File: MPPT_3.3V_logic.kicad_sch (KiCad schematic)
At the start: 42 parts, among them Q1 SIR5607DP-T1-RE3, Q2 SIR5607DP-T1-RE3, Q3 SIR5607DP-T1-RE3, Q4 SIR5607DP-T1-RE3, U1 LTC4417HUF, U2 TPS259470ARPWR, U3 TPS62177DQCR

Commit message: Started layout of the Ideal diode input (LTC4417)
I'm considering getting rid of the second 3V3 buck but will need to weigh the pros and cons a little more before commiting
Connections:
- net Solar_+X renamed OR'd_VOUT
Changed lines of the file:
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@@
 			"QQBLAE0AaABLAEEAQQBBAEEAQQBBAEEAQQBGAEcAUQBsAEEAQQBBAEEAQQBBAEEAQQBDAHIASQBT"
 			"AEEAQQBBAEEAQQBBAEEAQQBCAFYAawBKAEEAQQBBAEEAQQBBAEMAQQBnAHEAdwBFAEEAQQBBAEEA"
-			"QQBBAEIAQQBRAFYAWQBDAEEAQQBBAEEAQQBBAEMAZwBJAEMAcwBCAEEAQQBBAEEAQQBBAEIAUQ=="
+			"QQBBAEIAQQBRAFYAWQBDAEEAQQBBAEEAQQBBAEMAZwBJAEMAcwBCAEEAQQBBAEEAQQBBAEIAUQAv"
+			"AFEASQAyAGMAbgArAGYAQQBMAFAAQQBBAGcAQgBhAEQAVgBrAEoAQQBBAEEAQQBFAEUANgBUAC8A"
+			"bQBtAHkALwB3AHIAQgBFADYAWQAvAGYAbQArADMAZQB4AHMAVgBqAHAAdwA4AEsAaQA0ACsAcgBs"
+			"AEgAaABvAEoASABKAFMAUQA4AC8AZQBBAHYANwBCAHcAQwA0AG0AVQA1AEwAbAB5ADUAdAA2AHoA"
+			"NgBnAC8AYgBwAHkAOQBjAHAAWAAzADMAegBWADEAcgAwAEEAQQBBAEQAbwBTAEwAcgBlADAAMwBY"
+			"AFEAcQBPAFIATABGAHkANQBkAHYAWABKAFYAUgBPADcAdgBjAC8AOAAvAC8AUABDAHAAQgAxAE0A"
+			"RwArAE4AZQBNADYAQgBTAGgASABUADMANABlAHUAMQAxADEAMgBWAFgAegBkAFcAYQA3AGoAMgA3"
+			"AGoALwBvAEgALwBXAFAAZgBlADYAegBWAHUAdwB5AGcAOQBRAHoAdABPADEAVABWAHUAWABHAGMA"
+			"aQB2AGIAbQByAHUAdgBYAHIANwBkADEASAA5AEIAKwBuAGIAdAA0AGYAcwBPAG4ARwA5AHEANgBG"
+			"AHcAQQBBAEEAQQBCAHcAbQA1AGgAcABlAEUANQA5AHQANwBxAHQAZQA0AEcAYgA0AEIANABjAEEA"
+			"QQBBAEEAQQBBAEEAQQBCAFYAawBKAEEAQQBBAEEAQQBBAEMAQQBnAHEAdwBFAEEAQQBBAEEAQQBB"
+			"AEIAQQBRAFYAWQBDAEEAQQBBAEEAQQBBAEMAZwBpAEcAegByAEQAZwBBAEEAQQBBAEMAMwBvAFcA"
+			"cABuAGQAYwBXAHgAOABoAHAAWABUAFcAeQB2ADcAdgA0AEwAQQA5AGQAWAA0ADcAcABhAGYAcQB6"
+			"AGkANAB2AGsATAAzAFQAVAAzADkAZQBqAGQASQA3AEkAegBmADYASQBEAFEAQgB2AGoASAAyAEkA"
+			"QQBBAEEAQQBnAHoARAA3AGIAdABzAGYAeQB3AFMANQAzAGoAZAB2AHoAdABQACsAUQB4AE0AbgBQ"
+			"AEcAYQBQAFUAVQBmADQAMQBqAHgANABvAC8AVwBqAEQAWAB5ACsAYwB2ACsAQgA1AEcAdABNAGoA"
+			"NQBzAGsAZgBQAGQAVwBqADkALwAyAHQAMQAxAGMAQQBnAEIALwB1AHcAUQBFAEEAQQBBAEQAQwB5"
+			"AGYATABoAHIAaAAxAC8ALwByAFEAdQBLAEIARwBSAG8AdwBkAEsALwA3ADUAbABwADMALwBOAFEA"
+			"LwB1ACsALwB1AEEAUAA3ADkAYwBGAEoAUwBKAFMAZQBiAHIAUwB2AFAARwBUAHkAdABPAFYAcg=="
 		)
 	)
@@
 		)
 	)
-	(hierarchical_label "Solar_+X"
+	(hierarchical_label "OR'd_VOUT"
 		(shape input)
 		(at 33.02 95.25 180)

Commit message: Efuses for this board and Battery board
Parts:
- removed L1: 10uH, zLibrary:IND_BOURNS_SRR6038, symbol Device:L
- removed U3: TPS62177DQCR, zLibrary:DQC0010A, symbol TPS62177:TPS62175DQCR
- added R19, R20, R21: 100k, Resistor_SMD:R_0603_1608Metric, symbol Device:R
- added R22, R23: 10k, Resistor_SMD:R_0805_2012Metric, symbol Device:R
- added U3: TPS259470ARPWR, zLibrary:RPW0010A-MFG, symbol TPS259470:TPS259470ARPWR
- C10: value 100pF -> 2.2nF; MANUFACTURER_PART_NUMBER 885342206001 -> GCM1885C1H222FA16D
- C11: value 1uF -> 2.2nF; MANUFACTURER_PART_NUMBER CL10B105KQ8NNNC -> GCM1885C1H222FA16D
- C12: value 22uF -> 100pF; footprint zLibrary:CAP_C2220C_2S_KEM-M -> Capacitor_SMD:C_0603_1608Metric; MANUFACTURER_PART_NUMBER C2220C226MMR2L7289 -> 885342206001
- C13: value 100nF -> 100pF; MANUFACTURER_PART_NUMBER 06035C104K4T2A -> 885342206001
- C14, C15: value 22uF -> 10uF; footprint zLibrary:CAP_C2220C_2S_KEM-M -> Capacitor_SMD:C_1206_3216Metric; MANUFACTURER_PART_NUMBER C2220C226MMR2L7289 -> AVX, 04025C104KAT2A
- C9: value 2.2nF -> 100nF; MANUFACTURER_PART_NUMBER GCM1885C1H222FA16D -> 06035C104K4T2A
- R14: value 350k -> 182k; MANUFACTURER Digikey -> (none); MANUFACTURER_PART_NUMBER RN73R1JTTD3483F25 -> (none)
- R15, R18: value 100k -> 20k; MANUFACTURER Digikey -> (none); MANUFACTURER_PART_NUMBER AT0603FRE07100KL -> (none)
- R16: value 5k -> 100k; MANUFACTURER_PART_NUMBER RN73R1JTTD4991F100 -> AT0603FRE07100KL
- R17: value 100k -> 182k; MANUFACTURER Digikey -> (none); MANUFACTURER_PART_NUMBER AT0603FRE07100KL -> (none)
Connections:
- net +3.3V: now also R20.1, R21.1, U3.6 (OUT); no longer C14.1, R15.1, R17.1, R18.1
- net GND: now also U2.3 (AUXOFF), R19.2, R22.2, R23.2, U3.3 (AUXOFF), U3.8 (GND); no longer U2.2 (OVLO)
- net VIN_Out: now reaches C6.1, C7.1, Q1.5 (D), Q4.5 (D), U1.12 (VOUT)
- net VIN_Out: no longer C8.1, R14.1, U2.5 (IN)
- net at R14.2, U2.1 (EN_UVLO): now also R15.1
- net at R18.2: now also R19.1, U3.2 (OVLO)
- net at R17.2: now also R18.1, U3.1 (EN_UVLO); no longer U2.3 (AUXOFF)
- net at U2.10 (ITIMER): now also C10.1; no longer C9.1
- net at R15.2: now also R16.1, U2.2 (OVLO); no longer U2.4 (!FLT)
- net at U2.7 (dVdt): now also C12.1; no longer C10.1
- net at U2.9 (ILM): now also R22.1; no longer R16.1
- new net: R21.2, U3.4 (!FLT)
- new net: C11.1, U3.10 (ITIMER)
- new net: R20.2, U2.4 (!FLT)
- new net: R23.1, U3.9 (ILM)
- new net: C13.1, U3.7 (dVdt)
- new net 3V3_In: C8.1, C9.1, R14.1, R17.1, U2.5 (IN), U3.5 (IN)
- new net 3V3_Out_Batt: C14.1, U2.6 (OUT)
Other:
- note added: "E-Fuses"
- note added: "To Battery Board"
- note added: "To MPPT Board"
- note removed: "Buck Converter For On-Board 3.3V Logic"
- note removed: "E-Fuse"

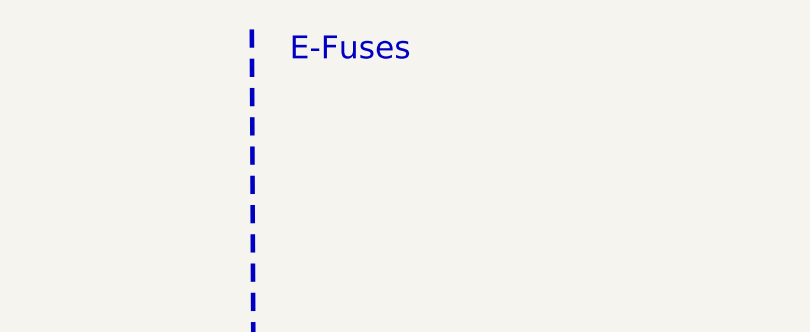
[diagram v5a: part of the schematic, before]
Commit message: Added Batt 1 and Batt 2 charging
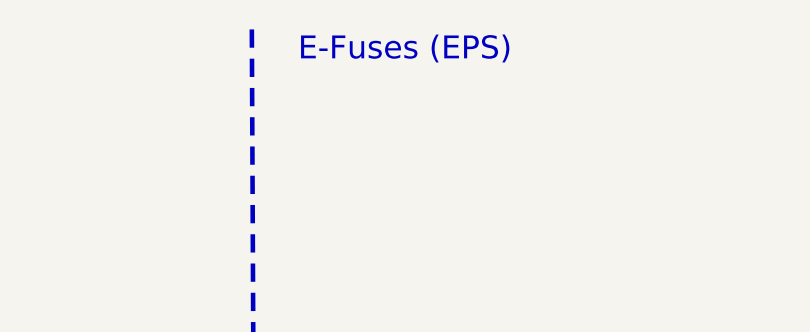
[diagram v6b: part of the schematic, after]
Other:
- note added: "E-Fuses (EPS)"
- note removed: "E-Fuses"
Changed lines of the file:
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@@
 		)
 	)
-	(text "E-Fuses"
+	(text "E-Fuses (EPS)"
 		(exclude_from_sim no)
-		(at 207.772 16.256 0)
+		(at 213.868 16.256 0)
 		(effects
 			(font
@@
 			"exQAZAWARmV0IEt1cnNpdgAAAAAAAAAAAAAAAAAA2/t5FABlBYBLYWzEsW4gxLB0YWxpawAAAAAA"
 			"AAAAAADZ+0cUAGYFgG5naGnDqm5nIMSRw6LMo20AAAAAAAAAAN/7RRQAZwWATG9kaSBldHphbmEA"
-			"AAAAAAAAAAAAAAAA3ftDFABoBYBJdMOhbGljbwAAAAAAAAAAAAAAAAAAAADT+0EUAGkFgAYAAA=="
+			"AAAAAAAAAAAAAAAA3ftDFABoBYBJdMOhbGljbwAAAAAAAAAAAAAAAAAAAADT+0EUAGkFgAYAAAAA"
+			"AAAAAAAAAAAAAAAAAAAAAAAAAAAAAAAAAAAAAAAAAAAAAAAAAAAAAAAAAAAAAAAAAAAAAAAAAAAA"
+			"AAAAAAAAAAAAAAAAAAAAAAAAAAAAAAAAAAAAAAAAAAAAAAAAAAAAAAAAAAAAAAAAAAAAAAAAAAAA"
+			"AAAAAAAAAAAAAAAAAAAAAAAAAAAAAAAAAAAAAAAAAAAAAAAAAAAAAAAAAAAAAAAAAAAAAAAAAAAA"
+			"AAAAAAAAAAAAAAAAAAAAAAAAAAAAAAAAAAAAAAAAAAAAAAAAAAAAAAAAAAAAAAAAAAAAAAAAAAAA"
+			"AAAAAAAAAAAAAAAAAAAAAAAAAAAAAAAAAAAAAAAAAAAAAAAAAAAAAAAAAAAAAAAAAAAAAAAAAAAA"
+			"AAAAAAAAAAAAAAAAAAAAAAAAAAAAAAAAAAAAAAAAAAAAAAAAAAAAAAAAAAAAAAAAAAAAAAAAAAAA"
+			"AAAAAAAAAAAAAAAAAAAAAAAAAAAAAAAAAAAAAAAAAAAAAAAAAAAAAAAAAAAAAAAAAAAAAAAAAAAA"
+			"AAAAAAAAAAAAAAAAAAAAAAAAAAAAAAAAAAAAAAAAAAAAAAAAAAAAAAAAAAAAAAAAAAAAAAAAAAAA"
+			"AAAAAAAAAAAAAAAAAAAAAAAAAAAAAAAAAAAAAAAAAAAAAAAAAAAAAAAAAAAAAAAAAAAAAAAAAAAA"
+			"AAAAAAAAAAAAAAAAAAAAAAAAAAAAAAAAAAAAAAAAAAAAAAAAAAAAAAAAAAAAAAAAAAAAAAAAAAAA"
+			"AAAAAAAAAAAAAAAAAAAAAAAAAAAAAAAAAAAAAAAAAAAAAAAAAAAAAAAAAAAAAAAAAAAAAAAAAAAA"
+			"AAAAAAAAAAAAAAAAAAAAAAAAAAAAAAAAAAAAAAAAAAAAAAAAAAAAAAAAAAAAAAAAAAAAAAAAAAAA"
+			"AAAAAAAAAAAAAAAAAAAAAAAAAAAAAAAAAAAAAAAAAAAAAAAAAAAAAAAAAAAAAAAAAAAAAAAAAAAA"
+			"AAAAAAAAAAAAAAAAAAAAAAAAAAAAAAAAAAAAAAAAAAAAAAAAAAAAAAAAAAAAAAAAAAAAAAAAAAAA"
+			"AAAAAAAAAAAAAAAAAAAAAAAAAAAAAAAAAAAAAAAAAAAAAAAAAAAAAAAAAAAAAAAAAAAAAAAAAAAA"
+			"AAAAAAAAAAAAAAAAAAAAAAAAAAAAAAAAAAAAAAAAAAAAAAAAAAAAAAAAAAAAAAAAAAAAAAAAAAAA"
+			"AAAAAAAAAAAAAAAAAAAAAAAAAAAAAAAAAAAAAAAAAAAAAAAAAAAAAAAAAAAAAAAAAAAAAAAAAAAA"
+			"AAAAAAAAAAAAAAAAAAAAAAAAAAAAAAAAAAAAAAAAAAAAAAAAAAAAAAAAAAAAAAAAAAAAAAAAAA=="
 		)
 	)
